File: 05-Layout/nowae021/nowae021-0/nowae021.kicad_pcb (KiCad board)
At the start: 2 copper layers, 21.6 x 20.3 mm, 41 parts, among them P1 NVT_BUS, P2 NVT_BUS, P3 SWD, Q1 PDTC123EU, Q2 PDTC123EU, Q3 PDTC123EU, Q4 PDTC123EU, Q5 PDTC123EU, Q6 PDTC123EU, SW1 BUTTON-WE_434153017835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

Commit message: Fixed error in led direction (nowae021-0)
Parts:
- turned DL1 to 0 degrees
- turned DL2 to 0 degrees
- turned DL3 to 0 degrees
- turned DL4 to 180 degrees
- turned DL5 to 180 degrees
- turned DL6 to 180 degrees
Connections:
- Q1 pad 3: Net-(DL1-Pad2) -> Net-(DL1-Pad1)
- Q2 pad 3: Net-(DL2-Pad2) -> Net-(DL2-Pad1)
- Q3 pad 3: Net-(DL3-Pad2) -> Net-(DL3-Pad1)
- Q4 pad 3: Net-(DL4-Pad2) -> Net-(DL4-Pad1)
- Q5 pad 3: Net-(DL5-Pad2) -> Net-(DL5-Pad1)
- Q6 pad 3: Net-(DL6-Pad2) -> Net-(DL6-Pad1)
- R1 pad 2: Net-(DL1-Pad1) -> Net-(DL1-Pad2)
- R2 pad 2: Net-(DL2-Pad1) -> Net-(DL2-Pad2)
- R3 pad 2: Net-(DL3-Pad1) -> Net-(DL3-Pad2)
- R4 pad 2: Net-(DL4-Pad1) -> Net-(DL4-Pad2)
- R5 pad 2: Net-(DL5-Pad1) -> Net-(DL5-Pad2)
- R6 pad 2: Net-(DL6-Pad1) -> Net-(DL6-Pad2)
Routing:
- net Net-(DL5-Pad2): track 2.06 -> 5.67 mm
- net Net-(DL5-Pad1): track 5.67 -> 2.06 mm
- net Net-(DL1-Pad2): track 2.06 -> 5.66 mm
- net Net-(DL1-Pad1): track 5.66 -> 2.06 mm
- net Net-(DL3-Pad2): track 2.06 -> 5.64 mm
- net Net-(DL3-Pad1): track 5.64 -> 2.06 mm
- net Net-(DL2-Pad2): track 2.08 -> 5.66 mm
- net Net-(DL2-Pad1): track 5.66 -> 2.08 mm
- net Net-(DL6-Pad2): track 2.08 -> 5.43 mm
- net Net-(DL6-Pad1): track 5.43 -> 2.08 mm
- net Net-(DL4-Pad2): track 2.08 -> 5.22 mm
- net Net-(DL4-Pad1): track 5.22 -> 2.08 mm

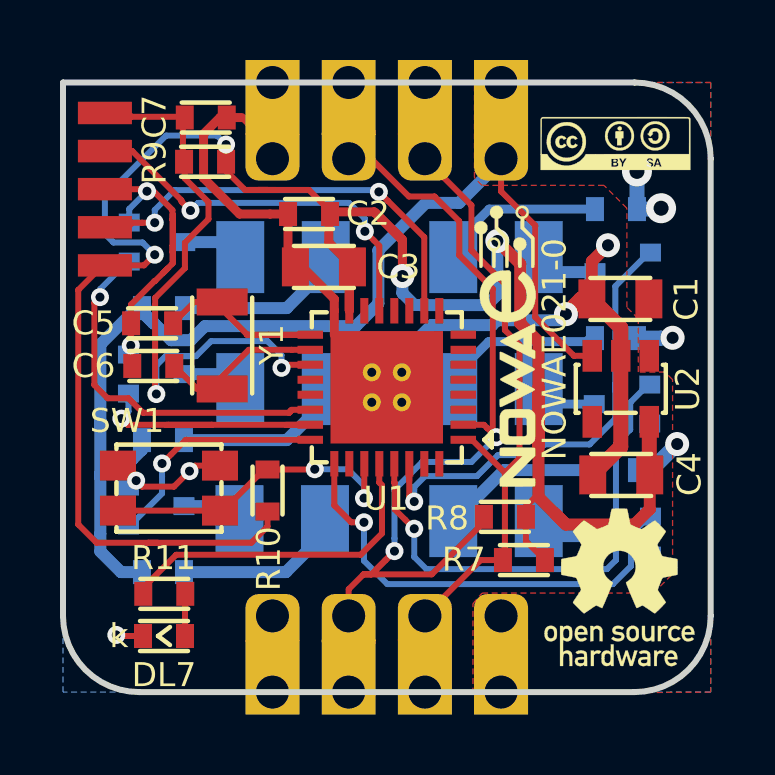
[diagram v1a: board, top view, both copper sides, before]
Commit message: Changed debug connetor to increase the robustness of copper (nowae021-0)
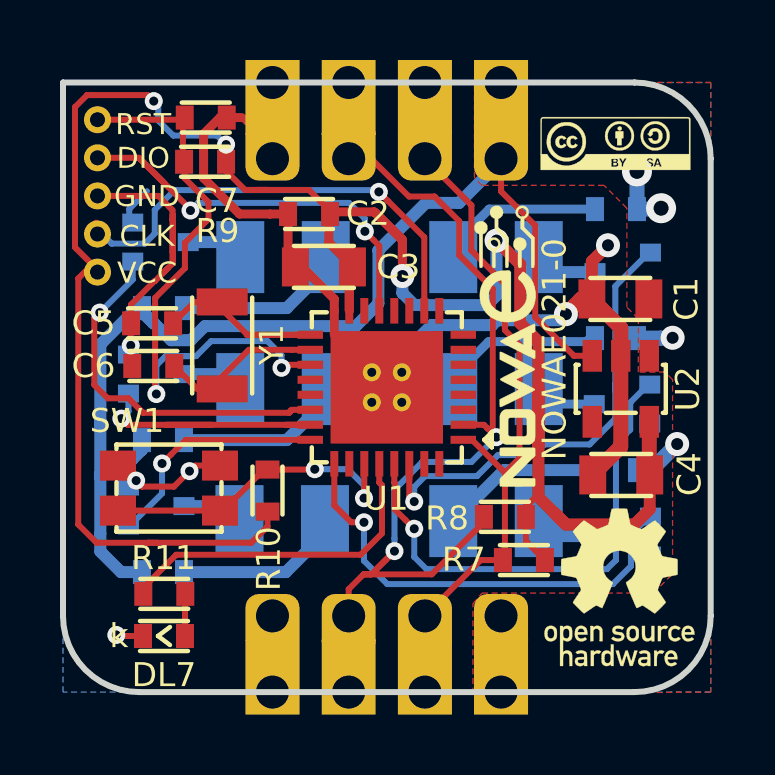
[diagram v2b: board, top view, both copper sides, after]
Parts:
- P3: footprint CONNECTOR:CONN-PAD-5x1-1.27 -> CONNECTOR:CONN-STRIP-5x1-1.27
- moved P3 0.33 mm to (103.2, 74.5)
- moved Q1 0.12 mm to (105.2, 76.0)
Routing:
- net /SWDIO: track 12.3 -> 15.0 mm
- net /SWCLK: track 13.9 -> 15.8 mm, vias 2 -> 1
- net /RESET: track 20.2 -> 21.5 mm
- net +3.3V: track 73.0 -> 74.1 mm
- net GND: track 59.3 -> 59.9 mm, vias 7 -> 6
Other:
- board text added: "CLK"
- board text added: "DIO"
- board text added: "GND"
- board text added: "RST"
- board text added: "VCC"

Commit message: Small fix on PCB file
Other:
- rule pad_to_mask_clearance: 0.051 -> 0
- rule solder_mask_min_width: 0.25 -> 0.15
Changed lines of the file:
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@@
     (pad_size 1.524 1.524)
     (pad_drill 0.762)
-    (pad_to_mask_clearance 0.051)
-    (solder_mask_min_width 0.25)
+    (pad_to_mask_clearance 0)
+    (solder_mask_min_width 0.15)
     (aux_axis_origin 102 91)
     (grid_origin 102 91)
@@
     (pcbplotparams
       (layerselection 0x010fc_ffffffff)
-      (usegerberextensions false)
+      (usegerberextensions true)
       (usegerberattributes false)
       (usegerberadvancedattributes false)

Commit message: Removed castellated holes from the PCB... it is not useful in this project and it is o expensive!
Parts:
- P1, P2: footprint CONNECTOR:CONN-HALFHOLE-4x1-2.54 -> CONNECTOR:CONN-STRIP-4x1-2.54_NOSILK
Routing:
- net GND: track 59.9 -> 56.5 mm
- net /NTV_COMM_SCL: track 32.0 -> 29.6 mm
- net +VIN: track 50.2 -> 49.1 mm
- net /NTV_COMM_SDA: track 24.2 -> 23.2 mm
